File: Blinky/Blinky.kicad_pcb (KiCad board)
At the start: 2 copper layers, 40.1 x 64.6 mm, 57 parts, among them J1 Conn_01x04_Pin, J2 Conn_01x03_Pin, J3 Battery Connector, J4 Charging Notches, J5 Speaker Connector, Q1 IRLML6244, Q2 IRLML6244, Q3 IRLML6244, Q4 IRLML6244, Q5 IRLML6244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

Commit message: version 1.9
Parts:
- removed C5, C9: 0.1uF, Capacitor_SMD:C_0603_1608Metric
- removed J5: Speaker Connector, footprint:CONN-TH_B2B-PH-K-S
- removed SW1: SK12D07VG4, otherfootprint:SW-TH_SK12D07VG4
- added R26: 1k, Resistor_SMD:R_0603_1608Metric, F.Cu at (161.6, 86.4)
- added R27: 100k, Resistor_SMD:R_0603_1608Metric, F.Cu at (130.5, 97.0)
- added R28: 100k, Resistor_SMD:R_0603_1608Metric, F.Cu at (130.5, 98.5)
- added R29: 10k, Resistor_SMD:R_0603_1608Metric, F.Cu at (130.4, 101.7)
- added U11: TS-1187A-B-A-B, footprint:SW-SMD_4P-L5.1-W5.1-P3.70-LS6.5-TL-2, F.Cu at (136.2, 79.1)
- added U12: MK-12C02-G025, footprint:SW-SMD_MK-12C02-G025, F.Cu at (157.7, 107.0)
- C2: value 1uf -> 220nf
- C3: value 1uf -> 100nf
- C4: value 100uF -> 100nf
- J1: value Conn_01x04_Pin -> Conn_01x06_Socket; footprint Connector_PinHeader_2.54mm:PinHeader_1x04_P2.54mm_Vertical -> Connector_PinSocket_2.54mm:PinSocket_1x06_P2.54mm_Vertical
- J2: value Conn_01x03_Pin -> Conn_01x06_Socket; footprint Connector_PinHeader_2.54mm:PinHeader_1x03_P2.54mm_Vertical -> Connector_PinSocket_2.54mm:PinSocket_1x06_P2.54mm_Vertical
- R19: value 100 -> 10k
- R24: value 3k3 -> 1k
- R25: value 1k -> 10k
- U4: value ZTS6156 -> LM358_C5296727; footprint footprint:MIC-SMD_3P-L2.8-W1.9_ZTS6056 -> footprint:SO-8_L4.9-W3.9-P1.27-LS6.0-BL
- U7: value PAM8304ASR -> B4013AM423-093; footprint footprint:MSOP-8_L3.0-W3.0-P0.65-LS5.0-BL -> footprint:MIC-TH_BD6.0_B6027AP383-056
- moved C4 34.6 mm to (130.5, 100.0)
- moved R24 33.5 mm to (159.6, 102.0), turned to 0 degrees
- moved R25 28.4 mm to (160.0, 89.3), turned to 0 degrees
- moved C6 24.3 mm to (160.9, 79.6), turned to 180 degrees
- moved C3 23.2 mm to (160.9, 83.7), turned to 180 degrees
- moved U7 22.1 mm to (131.4, 104.7)
- moved J2 13.3 mm to (164.9, 81.8), turned to 0 degrees
- moved R21 10.9 mm to (166.1, 102.4)
- moved J1 9.10 mm to (130.7, 81.8)
- moved U4 8.28 mm to (160.0, 95.1)
- moved C2 7.14 mm to (156.0, 96.9), turned to -90 degrees
- moved R19 6.86 mm to (159.6, 103.5), turned to 180 degrees
- moved C7 5.63 mm to (163.0, 102.5), turned to 0 degrees
- moved U5 4.81 mm to (164.7, 100.3), turned to 0 degrees
- moved J3 2.21 mm to (165.2, 105.4)
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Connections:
- C2 pad 1: GND -> /MIC
- C3 pad 2: VBAT -> VDD
- C4 pad 1: GND -> Net-(C4-Pad1)
- C4 pad 2: VBAT -> Net-(U7-+)
- J1 pad 2: /RxD -> unconnected-(J1-Pin_2-Pad2)
- J1 pad 3: /TxD -> unconnected-(J1-Pin_3-Pad3)
- J1 pad 4: GND -> unconnected-(J1-Pin_4-Pad4)
- J2 pad 1: GND -> unconnected-(J2-Pin_1-Pad1)
- J2 pad 2: VDD -> unconnected-(J2-Pin_2-Pad2)
- J2 pad 3: Net-(J2-Pin_3) -> unconnected-(J2-Pin_3-Pad3)
- R19 pad 1: /MIC_POWER -> Net-(U4A-IN1-)
- R24 pad 1: /SOUND -> Net-(U4A-IN1-)
- R24 pad 2: Net-(C9-Pad2) -> GND
- R25 pad 1: Net-(C9-Pad2) -> Net-(U4A-IN1+)
- R25 pad 2: GND -> Net-(U4B-IN2-)
- U3 pad 10: /MIC_POWER -> unconnected-(U3-IO17-Pad10)
- U3 pad 13: /BLUE1 -> unconnected-(U3-IO19-Pad13)
- U3 pad 14: /RED2 -> unconnected-(U3-IO20-Pad14)
- U3 pad 25: /SOUND -> unconnected-(U3-IO34-Pad25)
- U3 pad 26: /SOUND_ENABLE -> unconnected-(U3-IO45-Pad26)
- U3 pad 27: Net-(J2-Pin_3) -> /BOOT
- U3 pad 36: /RxD -> unconnected-(U3-RXD0-Pad36)
- U3 pad 37: /TxD -> unconnected-(U3-TXD0-Pad37)
- U4 pad 2: /MIC -> Net-(U4A-IN1-)
- U4 pad 3: GND -> Net-(U4A-IN1+)
- U7 pad 1: Net-(J5-Pin_1) -> Net-(U7-+)
- U7 pad 2: VBAT -> GND
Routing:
- net GND: track 301.0 -> 213.3 mm, vias 77 -> 51
- net /BLUE1: track 46.7 -> 10.3 mm
- net Net-(J2-Pin_3): track 35.1 -> 0.00 mm, vias 2 -> 0
- net Net-(U4B-IN2+): track 0.00 -> 34.6 mm, vias 0 -> 4
- net Net-(J5-Pin_2): track 25.5 -> 0.00 mm
- net VDD: track 158.6 -> 134.2 mm, vias 10 -> 11
- net Net-(J5-Pin_1): track 23.2 -> 0.00 mm
- net /RED2: track 35.7 -> 17.7 mm, vias 4 -> 2
- net /BAT+: track 69.8 -> 54.1 mm, vias 5 -> 0
- net Net-(C9-Pad2): track 11.6 -> 0.00 mm
- net /SOUND_ENABLE: track 11.4 -> 0.00 mm
- net /MIC_POWER: track 9.45 -> 0.00 mm
- net Net-(U4A-IN1+): track 0.00 -> 8.85 mm
- net /SOUND: track 7.87 -> 0.00 mm
- net Net-(U4A-IN1-): track 0.00 -> 7.43 mm
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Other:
- board size 40.1 x 64.6 mm -> 41.1 x 64.6 mm

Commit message: version 1.95
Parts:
- added USB1: MICROXNJ, footprint:MICRO-USB-SMD_MICROXNJ, F.Cu at (164.5, 49.8)
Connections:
- U3 pad 13: unconnected-(U3-IO19-Pad13) -> /USB-
- U3 pad 14: unconnected-(U3-IO20-Pad14) -> /USB+
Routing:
- net /USB+: track 0.00 -> 46.2 mm, vias 0 -> 6
- net /USB-: track 0.00 -> 42.6 mm, vias 0 -> 4
- net GND: track 213.3 -> 224.0 mm
- net CHARGE+: track 44.7 -> 54.3 mm, vias 4 -> 5

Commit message: removed gnd from back of led
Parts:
- added REF**: LED-SMD_XL-HD6070RGBC-A46L-BACKSIDE, footprint:LED-SMD_XL-HD6070RGBC-A46L-BACKSIDE, F.Cu at (152.3, 53.9)
- added REF**: LED-SMD_XL-HD6070RGBC-A46L-BACKSIDE, footprint:LED-SMD_XL-HD6070RGBC-A46L-BACKSIDE, B.Cu at (143.0, 54.0)
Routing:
- net GND: track 224.0 -> 199.8 mm, vias 51 -> 49

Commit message: connected pin headers to GPIOs
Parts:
- removed REF** (x2): LED-SMD_XL-HD6070RGBC-A46L-BACKSIDE, footprint:LED-SMD_XL-HD6070RGBC-A46L-BACKSIDE
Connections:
- J1 pad 2: unconnected-(J1-Pin_2-Pad2) -> /PIN32
- J1 pad 3: unconnected-(J1-Pin_3-Pad3) -> /PIN33
- J1 pad 4: unconnected-(J1-Pin_4-Pad4) -> /PIN34
- J1 pad 5: unconnected-(J1-Pin_5-Pad5) -> /PIN35
- J2 pad 1: unconnected-(J2-Pin_1-Pad1) -> /PIN10
- J2 pad 2: unconnected-(J2-Pin_2-Pad2) -> /PIN9
- J2 pad 3: unconnected-(J2-Pin_3-Pad3) -> /PIN8
- J2 pad 4: unconnected-(J2-Pin_4-Pad4) -> /PIN7
- J2 pad 5: unconnected-(J2-Pin_5-Pad5) -> /PIN6
- J2 pad 6: unconnected-(J2-Pin_6-Pad6) -> GND
- R12 pad 2: /BLUE1 -> /RED1
- R13 pad 2: /BLUE2 -> /RED2
- R15 pad 2: /RED2 -> /BLUE2
- R16 pad 2: /BLUE1 -> /RED1
- R18 pad 2: /RED1 -> /BLUE1
- R2 pad 2: /BLUE2 -> /RED2
- R6 pad 2: /RED2 -> /BLUE2
- R8 pad 2: /RED1 -> /BLUE1
- U3 pad 10: unconnected-(U3-IO17-Pad10) -> /PIN10
- U3 pad 11: /RED1 -> /BLUE1
- U3 pad 17: /BLUE2 -> /RED2
- U3 pad 30: unconnected-(U3-IO37-Pad30) -> /BLUE2
- U3 pad 31: unconnected-(U3-IO38-Pad31) -> /RED1
- U3 pad 32: unconnected-(U3-IO39-Pad32) -> /PIN32
- U3 pad 33: unconnected-(U3-IO40-Pad33) -> /PIN33
- U3 pad 34: unconnected-(U3-IO41-Pad34) -> /PIN34
- U3 pad 35: unconnected-(U3-IO42-Pad35) -> /PIN35
- U3 pad 6: unconnected-(U3-IO6-Pad6) -> /PIN6
- U3 pad 7: unconnected-(U3-IO7-Pad7) -> /PIN7
- U3 pad 8: unconnected-(U3-IO15-Pad8) -> /PIN8
- U3 pad 9: unconnected-(U3-IO16-Pad9) -> /PIN9
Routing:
- net /BLUE1: track 10.3 -> 58.5 mm, vias 0 -> 3
- net /RED2: track 17.7 -> 43.0 mm
- net /RED1: track 59.4 -> 38.0 mm, vias 3 -> 2
- net /PIN10: track 0.00 -> 15.4 mm, vias 0 -> 2
- net /PIN9: track 0.00 -> 14.9 mm, vias 0 -> 2
- net /PIN8: track 0.00 -> 14.3 mm, vias 0 -> 2
- net /PIN6: track 0.00 -> 14.1 mm, vias 0 -> 2
- net /PIN7: track 0.00 -> 13.8 mm, vias 0 -> 2
- net /PIN32: track 0.00 -> 9.08 mm
- net /PIN33: track 0.00 -> 7.83 mm
- net GND: track 199.8 -> 206.9 mm
- net /BLUE2: track 43.0 -> 49.4 mm, vias 2 -> 4
- net /PIN34: track 0.00 -> 6.18 mm
- net /PIN35: track 0.00 -> 5.48 mm
- net VDD: track 134.2 -> 136.5 mm
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
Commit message: removed ground connection for LED backside, added flipside led copper
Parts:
- added U13: XL-HD6070RGBC-A46L, footprint:LED-SMD_XL-HD6070RGBC-A46L-BACKSIDE, B.Cu at (143.0, 54.0)
- added U14: XL-HD6070RGBC-A46L, footprint:LED-SMD_XL-HD6070RGBC-A46L-BACKSIDE, F.Cu at (152.3, 53.9)
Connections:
- U1 pad 7: GND -> unconnected-(U1-Pad7)
- U2 pad 7: GND -> unconnected-(U2-Pad7)
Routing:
- net GND: track 206.9 -> 203.5 mm, vias 49 -> 17
- net unconnected-(U1-Pad7): track 0.00 -> 2.70 mm
- net unconnected-(U2-Pad7): track 0.00 -> 0.70 mm

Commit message: added C after voltage reg
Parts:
- added C5: 470uf, Capacitor_SMD:C_0603_1608Metric, F.Cu at (159.7, 77.8)
- R1, R11: value 1 -> 4
- R3, R9: value 1 -> 2
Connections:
- C6 pad 2: VDD -> Net-(U8-Vout)
- C8 pad 2: VDD -> Net-(U8-Vout)
- U8 pad 3: VDD -> Net-(U8-Vout)
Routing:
- net VDD: track 136.5 -> 102.5 mm, vias 11 -> 7
- net Net-(U8-Vout): track 0.00 -> 29.6 mm, vias 0 -> 3

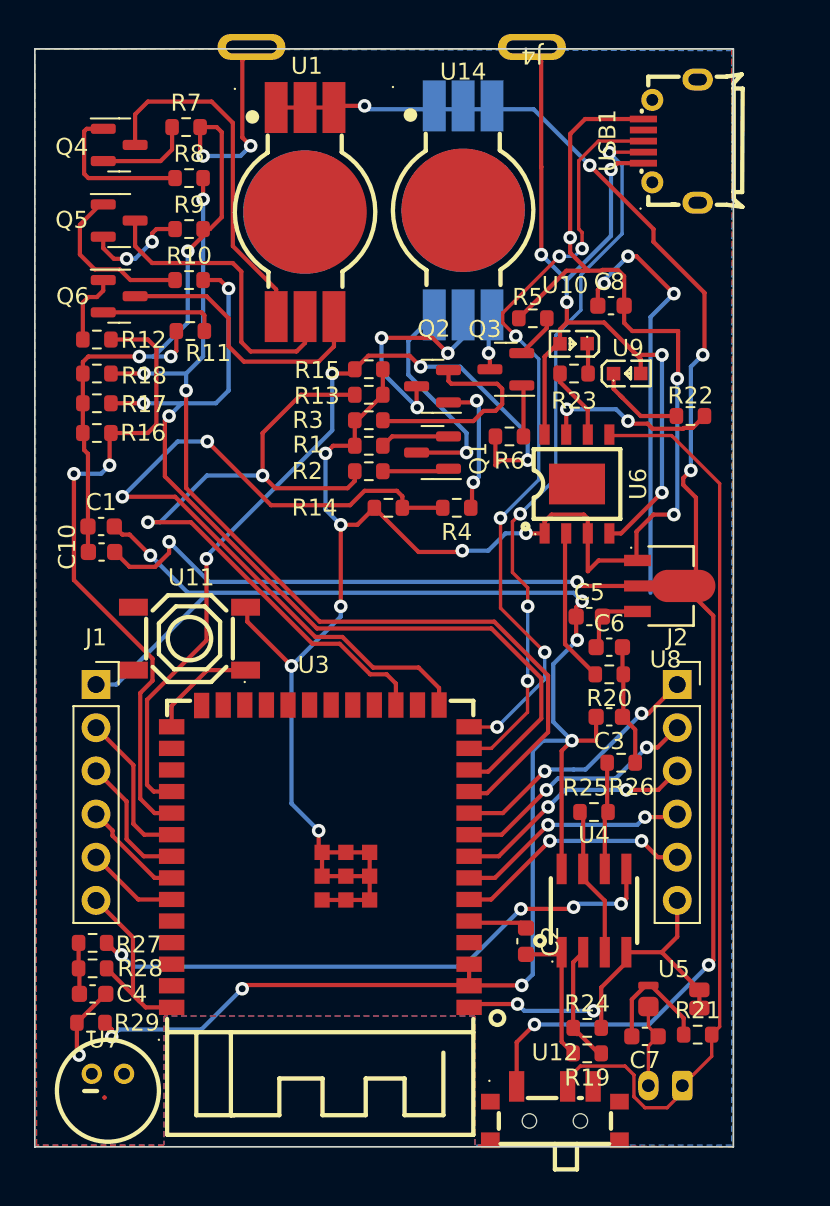
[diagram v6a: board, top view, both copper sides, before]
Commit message: fixed Vreg and Mic
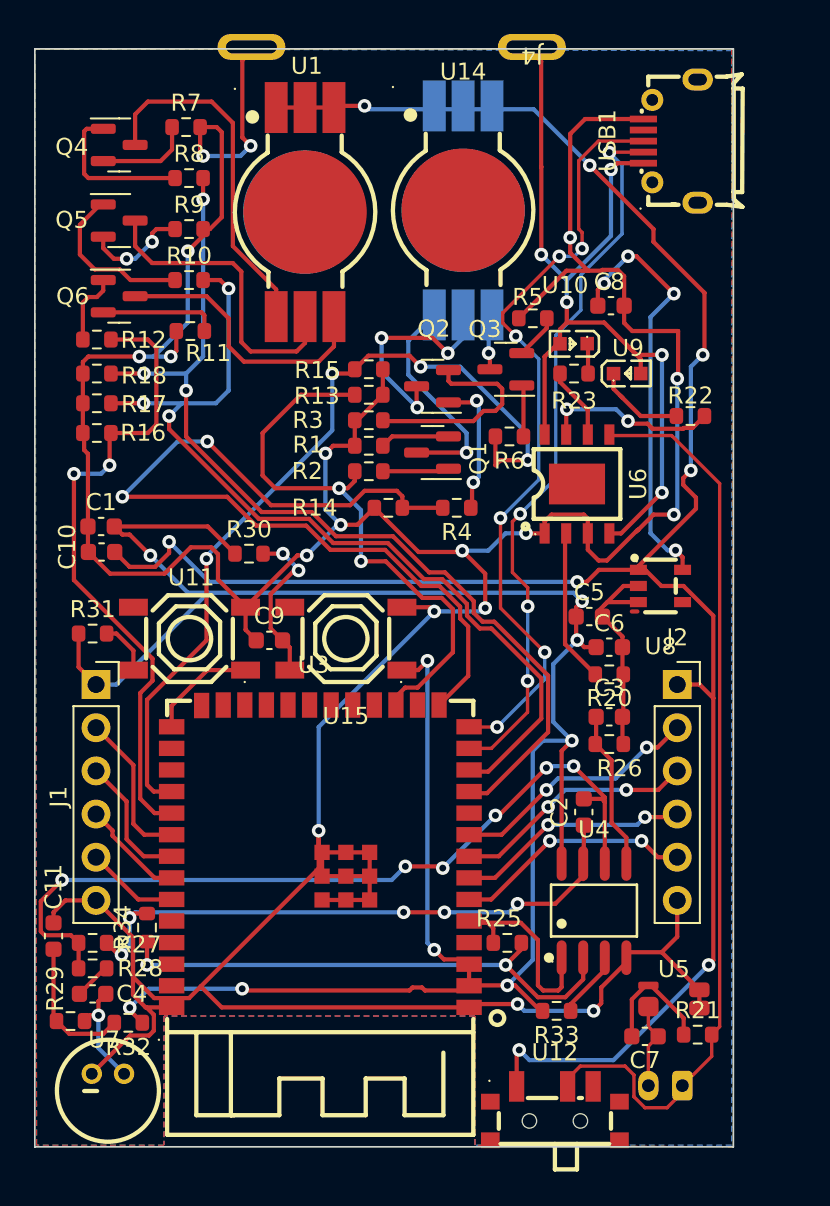
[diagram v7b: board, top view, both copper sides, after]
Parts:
- removed R19: 10k, Resistor_SMD:R_0603_1608Metric
- removed R24: 1k, Resistor_SMD:R_0603_1608Metric
- added C11: 1uF, Capacitor_SMD:C_0603_1608Metric, F.Cu at (128.2, 96.6)
- added C9: 1uf, Capacitor_SMD:C_0603_1608Metric, F.Cu at (140.9, 79.2)
- added R30: 100k, Resistor_SMD:R_0603_1608Metric, F.Cu at (139.7, 74.1)
- added R31: 100k, Resistor_SMD:R_0603_1608Metric, F.Cu at (130.5, 78.8)
- added R32: 470R, Resistor_SMD:R_0603_1608Metric, F.Cu at (132.6, 101.7)
- added R33: 100k, Resistor_SMD:R_0603_1608Metric, F.Cu at (157.8, 101.0)
- added R34: 10k, Resistor_SMD:R_0603_1608Metric, F.Cu at (133.7, 96.1)
- added U15: TS-1187A-B-A-B, footprint:SW-SMD_4P-L5.1-W5.1-P3.70-LS6.5-TL-2, F.Cu at (145.4, 79.1)
- C2: value 220nf -> 100pF optional
- C4: value 100nf -> 470nF
- R25: value 10k -> 100k
- R26: value 1k -> 47k
- R28: value 100k -> 10k
- R3, R5, R7, R9: value 2 -> 1
- U4: value LM358_C5296727 -> TLV9002IDR; footprint footprint:SO-8_L4.9-W3.9-P1.27-LS6.0-BL -> footprint:SOIC-8_L4.9-W3.9-P1.27-LS6.0-BL
- U8: value HT7833-A -> ME6217C33M5G; footprint otherfootprint:SOT-89-3_L4.5-W2.5-P1.50-LS4.2-BR -> footprint:SOT-23-5_L3.0-W1.7-P0.95-LS2.8-BR
- moved R25 9.24 mm to (154.9, 97.0)
- moved C2 8.33 mm to (159.4, 89.3), turned to 90 degrees
- moved R26 1.30 mm to (160.9, 85.3)
- moved R29 1.20 mm to (129.2, 101.6)
- turned C3 to 0 degrees
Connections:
- C2 pad 1: /MIC -> Net-(U4B-OUT2)
- C2 pad 2: Net-(U4A-OUT1) -> Net-(U4B-IN2-)
- C3 pad 1: GND -> /VDD_REF
- C3 pad 2: VDD -> GND
- C5 pad 2: Net-(U8-Vout) -> GND
- C6 pad 2: Net-(U8-Vout) -> VDD
- C8 pad 2: Net-(U8-Vout) -> VDD
- J2 pad 1: /PIN10 -> VBAT
- R25 pad 1: Net-(U4A-IN1+) -> /MIC
- R25 pad 2: Net-(U4B-IN2-) -> Net-(U4A-IN1-)
- R26 pad 2: Net-(U4B-IN2-) -> /VDD_REF
- R27 pad 1: Net-(C4-Pad1) -> Net-(U4B-IN2-)
- R27 pad 2: Net-(U4B-IN2+) -> Net-(U4B-OUT2)
- R28 pad 1: Net-(C4-Pad1) -> Net-(U4B-IN2-)
- R28 pad 2: GND -> Net-(C4-Pad1)
- R29 pad 1: Net-(U7-+) -> Net-(C11-Pad1)
- R29 pad 2: VDD -> Net-(U7-+)
- U11 pad 2: unconnected-(U11-B-Pad2) -> Net-(U11-B)
- U3 pad 3: VDD -> /EN
- U4 pad 1: Net-(U4A-OUT1) -> /MIC
- U4 pad 3: Net-(U4A-IN1+) -> /VDD_REF
- U4 pad 5: Net-(U4B-IN2+) -> /VDD_REF
- U4 pad 7: Net-(U4A-IN1+) -> Net-(U4B-OUT2)
- U8 pad 1: GND -> VBAT
- U8 pad 2: VBAT -> GND
- U8 pad 3: Net-(U8-Vout) -> GND
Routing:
- net GND: track 203.5 -> 271.5 mm, vias 17 -> 18
- net Net-(U4B-IN2-): track 6.35 -> 48.4 mm, vias 0 -> 6
- net Net-(U4B-OUT2): track 0.00 -> 36.0 mm, vias 0 -> 5
- net VDD: track 102.5 -> 138.1 mm, vias 7 -> 11
- net Net-(U4B-IN2+): track 34.6 -> 0.00 mm, vias 4 -> 0
- net Net-(U8-Vout): track 29.6 -> 0.00 mm, vias 3 -> 0
- net Net-(U4A-IN1-): track 7.43 -> 31.2 mm, vias 0 -> 2
- net /EN: track 0.00 -> 20.9 mm, vias 0 -> 2
- net /PIN10: track 15.4 -> 0.00 mm, vias 2 -> 0
- net /VDD_REF: track 0.00 -> 13.4 mm
- net Net-(U15-B): track 0.00 -> 9.70 mm, vias 0 -> 2
- net /MIC: track 3.52 -> 13.0 mm
- net Net-(U4A-IN1+): track 8.85 -> 0.00 mm
- net /RED2: track 43.0 -> 34.2 mm
- net Net-(U4A-OUT1): track 8.38 -> 0.00 mm
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
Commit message: fixed routing of u8 pin 3
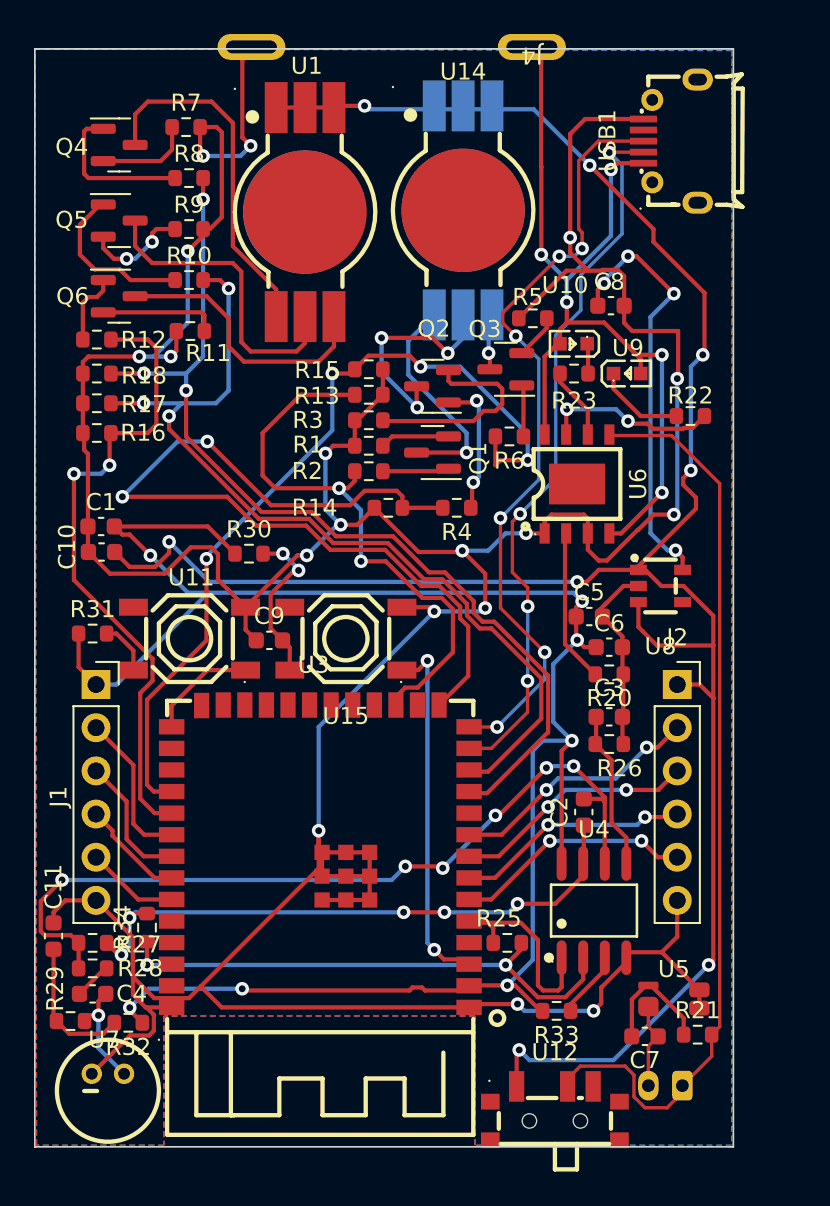
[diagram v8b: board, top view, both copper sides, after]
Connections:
- U8 pad 3: GND -> VBAT
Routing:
- net VBAT: track 126.8 -> 133.1 mm
- net unconnected-(U1-Pad7): track 2.70 -> 0.00 mm
- net GND: track 271.5 -> 269.5 mm
- net VDD: track 138.1 -> 136.8 mm
- net unconnected-(U2-Pad7): track 0.70 -> 0.00 mm
